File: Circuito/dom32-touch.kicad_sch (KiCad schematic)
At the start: 51 parts, among them J1 MEM2067-02-180-00-A, J2 Poste X 5, J3 MSP3218_LCD, J4 MSP3218_SD, J5 DEBUG, J6 POWER 5v, SW1 TactSwitch, U1 ZLDO1117QG33TADICT-ND, U2 PIC32MM0256GPM028-I-SS

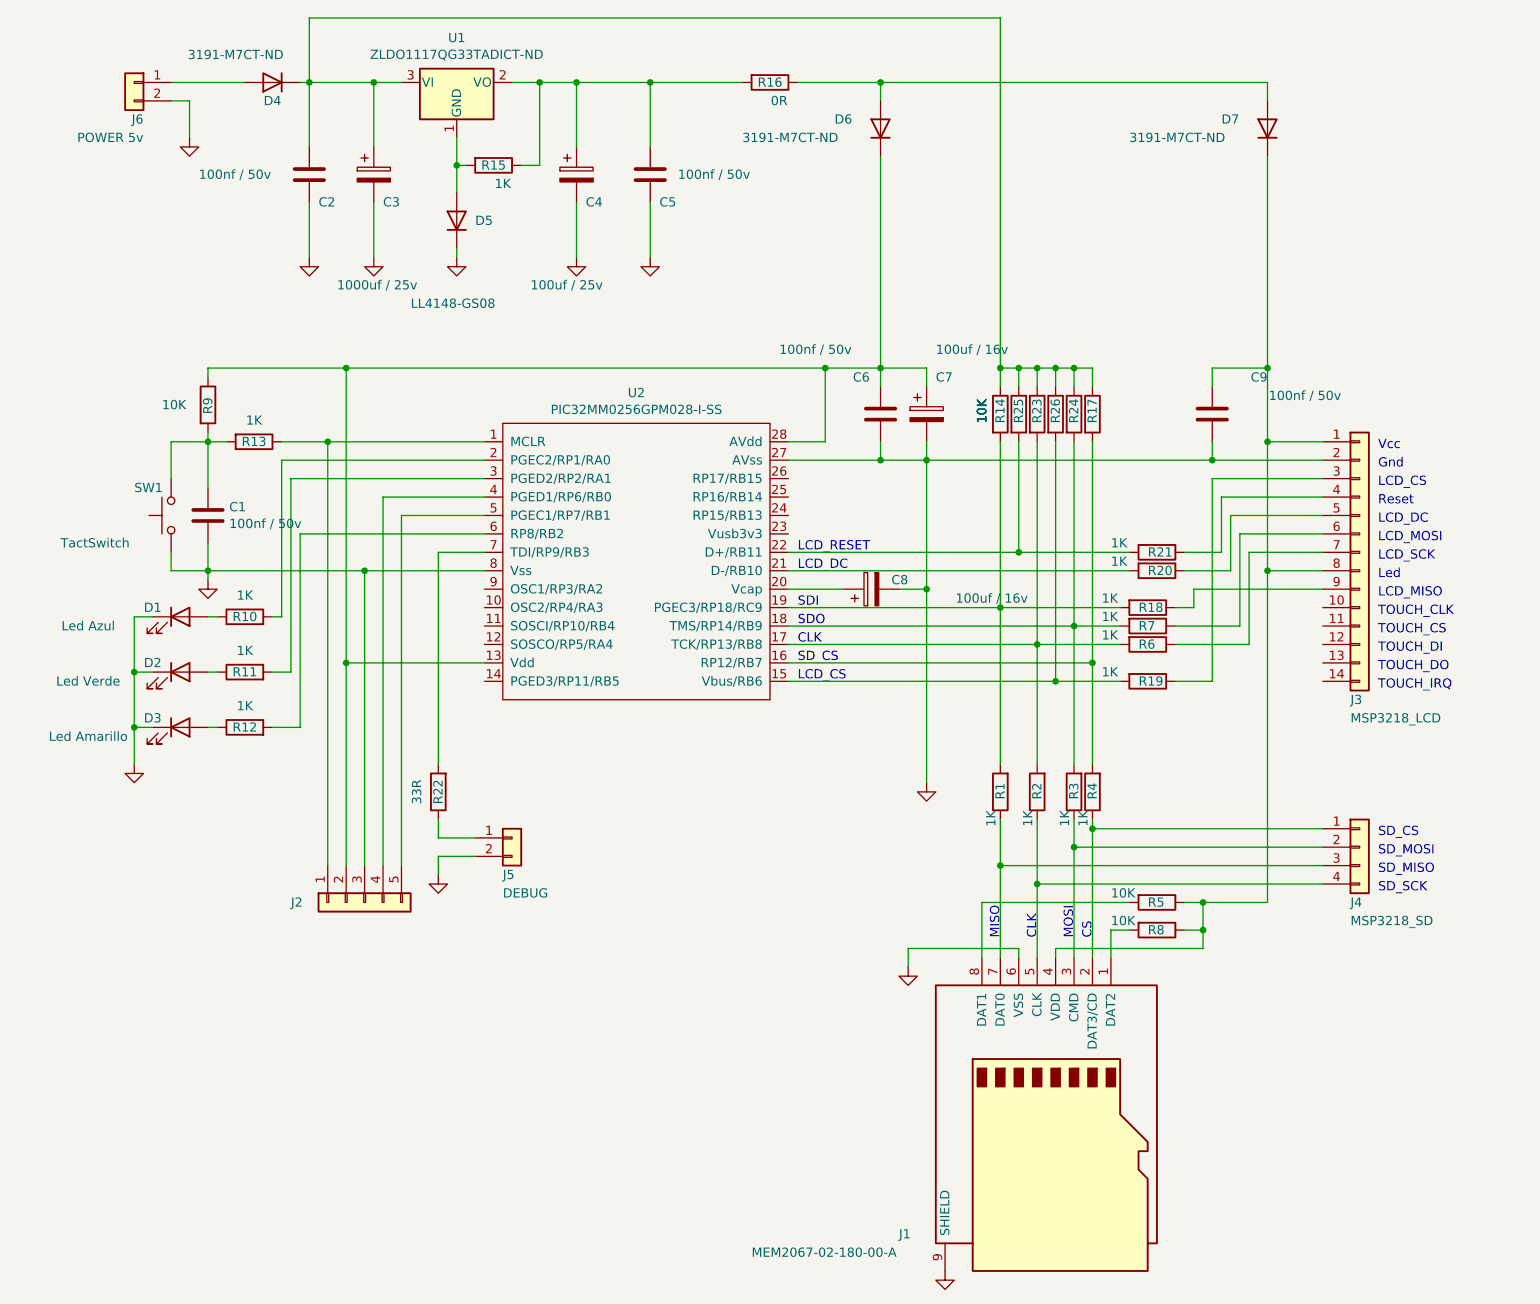
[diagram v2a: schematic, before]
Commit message: Pinta medio display
Pinta medio display
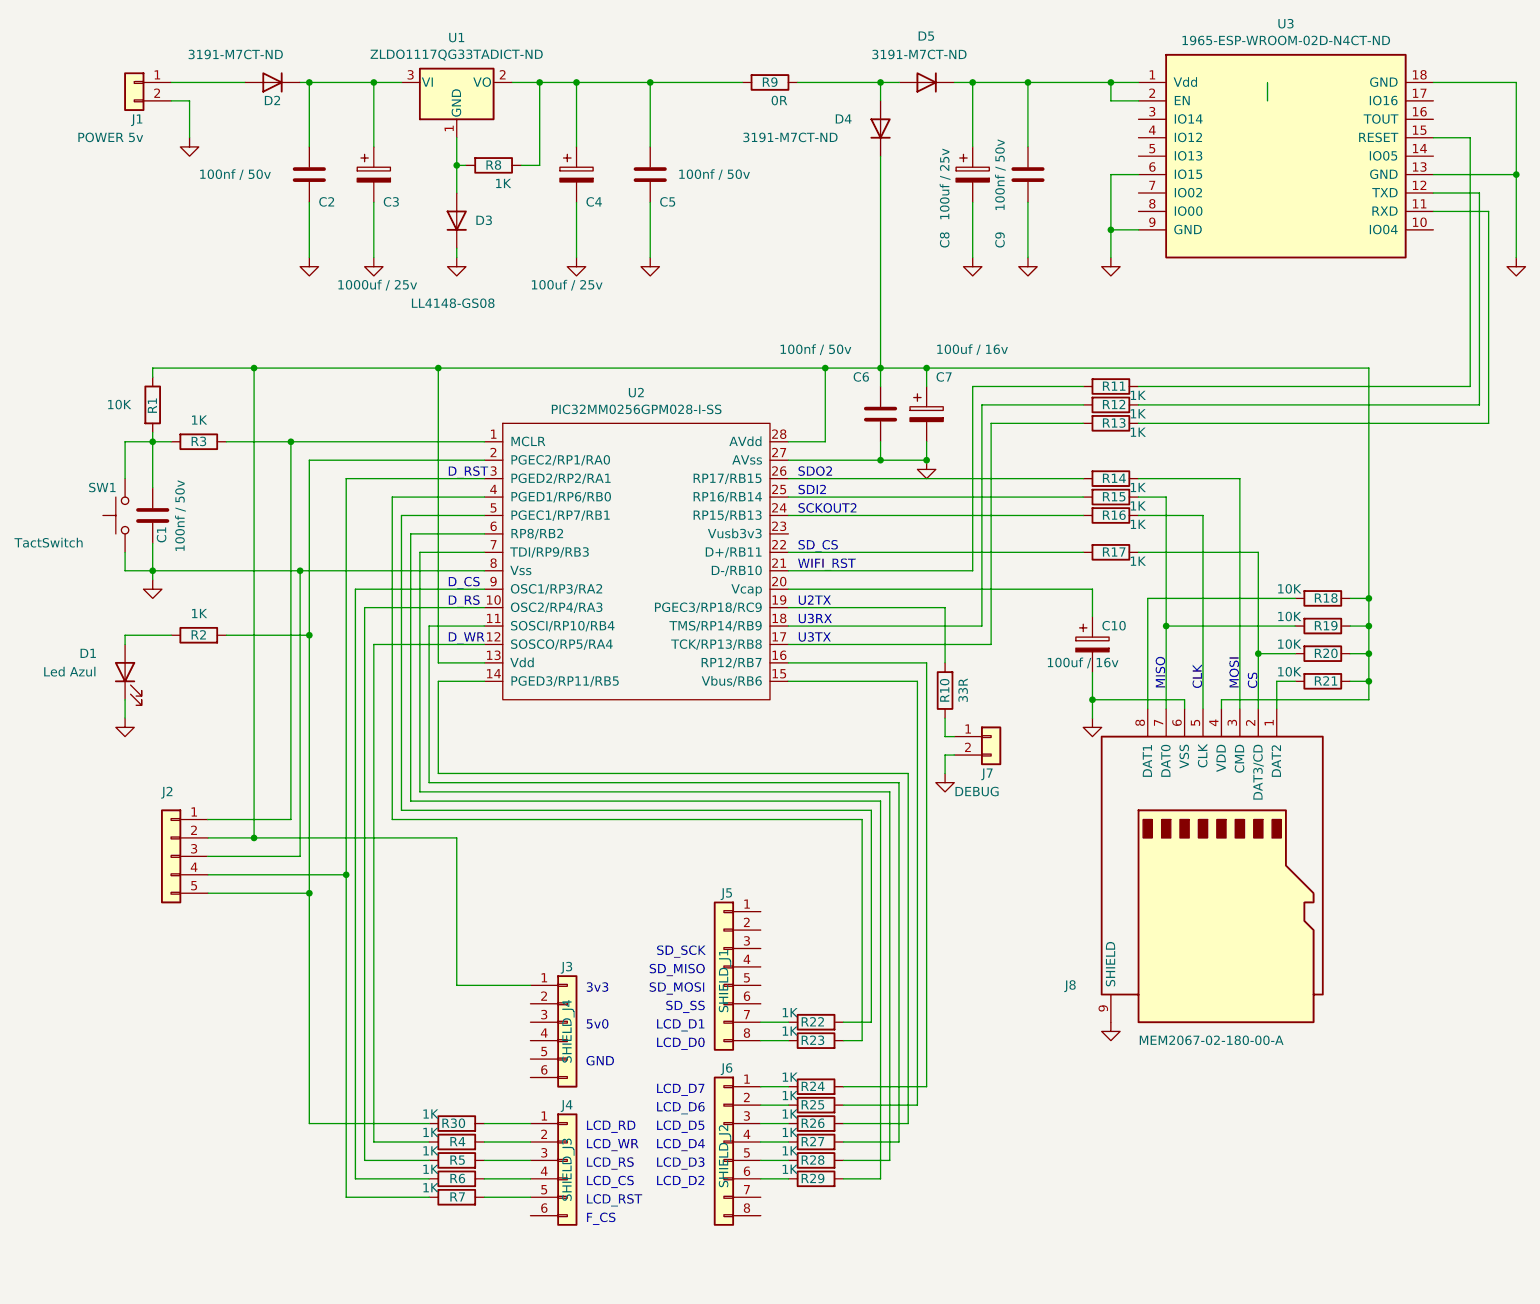
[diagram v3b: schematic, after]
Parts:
- removed D2: Led Verde, Diode_SMD:D_0805_2012Metric_Pad1.15x1.40mm_HandSolder, symbol Device:LED
- removed D3: Led Amarillo, Diode_SMD:D_0805_2012Metric_Pad1.15x1.40mm_HandSolder, symbol Device:LED
- removed D7: 3191-M7CT-ND, Diode_SMD:D_SMA, symbol Device:D
- removed J3: MSP3218_LCD, symbol Connector_Generic:Conn_01x14
- removed J4: MSP3218_SD, symbol Connector_Generic:Conn_01x04
- removed R14, R17: 10K, Resistor_SMD:R_0805_2012Metric_Pad1.20x1.40mm_HandSolder, symbol Device:R
- removed R20, R21: 1K, Resistor_SMD:R_0805_2012Metric_Pad1.20x1.40mm_HandSolder, symbol Device:R
- added C8: 100uf / 25v, Capacitor_THT:CP_Radial_D6.3mm_P2.50mm, symbol Device:C_Polarized
- added D5: 3191-M7CT-ND, Diode_SMD:D_SMA, symbol Device:D
- added J3: SHIELD_J4, symbol Connector_Generic:Conn_01x06
- added J4: SHIELD_J3, symbol Connector_Generic:Conn_01x06
- added J5: SHIELD_J1, symbol Connector_Generic:Conn_01x08
- added J6: SHIELD_J2, symbol Connector_Generic:Conn_01x08
- added R13, R22, R27, R28, R29, R30, R4, R5: 1K, Resistor_SMD:R_0805_2012Metric_Pad1.20x1.40mm_HandSolder, symbol Device:R
- added U3: 1965-ESP-WROOM-02D-N4CT-ND, RF_Module:ESP-WROOM-02, symbol DomIO32-rescue:ESP-02-DomIO32
- R18, R19: value 1K -> 10K
- R23, R24, R25, R26: value 10K -> 1K
- renumbered C8 to C10, D4 to D2, D5 to D3, D6 to D4, J6 to J1, J5 to J7, J1 to J8, R9 to R1, R22 to R10, R3 to R14, R1 to R15, R2 to R16, R4 to R17, R10 to R2, R5 to R20, R8 to R21, R13 to R3, R15 to R8, R16 to R9
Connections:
- net GND: now also C9.2, C8.2, U3.13 (GND), U3.18 (GND), U3.6 (IO15), U3.9 (GND); no longer C9.1
- net at C6.1, C7.1, D4.1 (K)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: now also J8.4 (VDD), R18.1, R19.1, R20.1, R21.1, J3.1 (Pin_1)
- net at J2.4 (Pin_4): now also R7.1, U2.3 (PGED2/RP2/RA1); no longer U2.4 (PGED1/RP6/RB0)
- net at J2.5 (Pin_5): now also R2.2, U2.2 (PGEC2/RP1/RA0), R30.1; no longer U2.5 (PGEC1/RP7/RB1)
- net at C2.1, C3.1, D2.1 (K)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: no longer R23.1, R24.1, R25.1, R26.1
- net at J8.2 (DAT3/CD), R17.1: now also R20.2
- net at J8.7 (DAT0), R15.1: now also R19.2
- net at R17.2: now also U2.22 (D+/RB11); no longer U2.16 (RP12/RB7)
- net at D4.2 (A), R9.1: now also D5.2 (A)
- net at R25.2: now also U2.15 (Vbus/RB6); no longer U2.22 (D+/RB11)
- net at U2.10 (OSC2/RP4/RA3): now also R5.1
- net at U2.11 (SOSCI/RP10/RB4): now also R27.2
- net at U2.12 (SOSCO/RP5/RA4): now also R4.1
- net at U2.14 (PGED3/RP11/RB5): now also R26.2
- net at U2.21 (D-/RB10): now also R11.2
- net at U2.24 (RP15/RB13): now also R16.2
- net at U2.25 (RP16/RB14): now also R15.2
- net at U2.26 (RP17/RB15): now also R14.2
- net at R12.2: now also U2.18 (TMS/RP14/RB9); no longer U2.6 (RP8/RB2)
- net at R10.2: now also U2.19 (PGEC3/RP18/RC9); no longer U2.7 (TDI/RP9/RB3)
- net at U2.9 (OSC1/RP3/RA2): now also R6.1
- net at J8.8 (DAT1): now also R18.2; no longer R20.2
- net at R11.1: now also U3.15 (RESET)
- net at R12.1: now also U3.12 (TXD)
- new net: J6.2 (Pin_2), R25.1
- new net: C8.1, C9.1, D5.1 (K), U3.1 (Vdd), U3.2 (EN)
- new net: J6.1 (Pin_1), R24.1
- new net: J6.3 (Pin_3), R26.1
- new net: J6.4 (Pin_4), R27.1
- new net: J6.5 (Pin_5), R28.1
- new net: J6.6 (Pin_6), R29.1
- new net: J4.5 (Pin_5), R7.2
- new net: R24.2, U2.16 (RP12/RB7)
- new net: R13.2, U2.17 (TCK/RP13/RB8)
- new net: R23.2, U2.4 (PGED1/RP6/RB0)
- new net: R22.2, U2.5 (PGEC1/RP7/RB1)
- new net: R29.2, U2.6 (RP8/RB2)
- new net: R28.2, U2.7 (TDI/RP9/RB3)
- new net: J5.8 (Pin_8), R23.1
- new net: J4.1 (Pin_1), R30.2
- new net: J4.2 (Pin_2), R4.2
- new net: J4.3 (Pin_3), R5.2
- new net: J4.4 (Pin_4), R6.2
- new net: R13.1, U3.11 (RXD)
- new net: J5.7 (Pin_7), R22.1
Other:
- note added: "3v3"
- note added: "5v0"
- note added: "D_CS"
- note added: "D_RS"
- note added: "D_RST"
- note added: "D_WR"
- note added: "F_CS"
- note added: "GND"
- note added: "LCD_D0"
- note added: "LCD_D1"
- note added: "LCD_D2"
- note added: "LCD_D3"
- note added: "LCD_D4"
- note added: "LCD_D5"
- note added: "LCD_D6"
- note added: "LCD_D7"
- note added: "LCD_RD"
- note added: "LCD_RS"
- note added: "LCD_RST"
- note added: "LCD_WR"
- note added: "SCKOUT2"
- note added: "SDI2"
- note added: "SDO2"
- note added: "SD_SS"
- note added: "U2TX"
- note added: "U3RX"
- note added: "U3TX"
- note added: "WIFI_RST"
- note removed: "Gnd"
- note removed: "LCD_DC"
- note removed: "LCD_MISO"
- note removed: "LCD_MOSI"
- note removed: "LCD_RESET"
- note removed: "LCD_SCK"
- note removed: "Led"
- note removed: "Reset"
- note removed: "SDI"
- note removed: "SDO"
- note removed: "TOUCH_CLK"
- note removed: "TOUCH_CS"
- note removed: "TOUCH_DI"
- note removed: "TOUCH_DO"
- note removed: "TOUCH_IRQ"
- note removed: "Vcc"
- moved on the sheet: C1, C10, D1, J2, J7, J8, R1, R10, R14, R15, R16, R17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

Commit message: Texto
Texto
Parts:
- removed R22, R23, R24, R25, R26, R27, R28, R29, R30, R4, R5, R6, R7: 1K, Resistor_SMD:R_0805_2012Metric_Pad1.20x1.40mm_HandSolder, symbol Device:R
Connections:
- net at J6.2 (Pin_2): now also U2.15 (Vbus/RB6)
- net at J2.4 (Pin_4), U2.3 (PGED2/RP2/RA1): now also J4.5 (Pin_5)
- net at J2.5 (Pin_5), R2.2, U2.2 (PGEC2/RP1/RA0): now also J4.1 (Pin_1)
- net at J6.1 (Pin_1): now also U2.16 (RP12/RB7)
- net at J6.3 (Pin_3): now also U2.14 (PGED3/RP11/RB5)
- net at J6.4 (Pin_4): now also U2.11 (SOSCI/RP10/RB4)
- net at J6.5 (Pin_5): now also U2.7 (TDI/RP9/RB3)
- net at J6.6 (Pin_6): now also U2.6 (RP8/RB2)
- net at R17.2, U2.22 (D+/RB11): now also J5.6 (Pin_6)
- net at R15.2, U2.25 (RP16/RB14): now also J5.4 (Pin_4)
- net at R14.2, U2.26 (RP17/RB15): now also J5.5 (Pin_5)
- net at U2.10 (OSC2/RP4/RA3): now also J4.3 (Pin_3)
- net at U2.12 (SOSCO/RP5/RA4): now also J4.2 (Pin_2)
- net at R16.2, U2.24 (RP15/RB13): now also J5.3 (Pin_3)
- net at U2.4 (PGED1/RP6/RB0): now also J5.8 (Pin_8)
- net at U2.5 (PGEC1/RP7/RB1): now also J5.7 (Pin_7)
- net at U2.9 (OSC1/RP3/RA2): now also J4.4 (Pin_4)
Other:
- note added: "D_RD"
- moved on the sheet: C1, C10, J2, J7, R10, R11, R12, R13, R14, R15, R16, R17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

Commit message: Boton con icono
Boton con icono
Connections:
- net GND: now also J3.5 (Pin_5)
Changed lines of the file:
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@@
+    (stroke (width 0) (type default))
+  )
+  (wire (pts (xy 87.63 163.83) (xy 85.09 163.83))
     (stroke (width 0) (type default))
   )
@@
   )
   (wire (pts (xy 198.12 115.57) (xy 198.12 114.3))
+    (stroke (width 0) (type default))
+  )
+  (wire (pts (xy 85.09 163.83) (xy 85.09 167.64))
     (stroke (width 0) (type default))
   )
@@
         )
       )
+    )
+  )
+  (symbol (lib_id "power:GND") (at 85.09 167.64 0) (unit 1)
+    (in_bom yes) (on_board yes) (dnp no)
+    (property "Reference" "#PWR017" (at 85.09 173.99 0)
+      (effects (font (size 1.27 1.27)) hide)
+    )
+    (property "Value" "GND" (at 85.217 172.0342 0)
+      (effects (font (size 1.27 1.27)) hide)
+    )
+    (property "Footprint" "" (at 85.09 167.64 0)
+      (effects (font (size 1.27 1.27)) hide)
+    )
+    (property "Datasheet" "" (at 85.09 167.64 0)
+      (effects (font (size 1.27 1.27)) hide)
+    )
+    (pin "1")
+    (instances
+      (project "dom32-touch"
+        (path "/52c02980-b5ea-450b-8d27-915fdca3d27d"
+          (reference "#PWR017") (unit 1)
+        )
+      )

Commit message: Agregado de modulo wifi
Agregado de modulo wifi
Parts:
- removed D1: Led Azul, Diode_SMD:D_0805_2012Metric_Pad1.15x1.40mm_HandSolder, symbol Device:LED
- removed J3: SHIELD_J4, symbol Connector_Generic:Conn_01x06
- removed J4: SHIELD_J3, symbol Connector_Generic:Conn_01x06
- removed J5: SHIELD_J1, symbol Connector_Generic:Conn_01x08
- removed J6: SHIELD_J2, symbol Connector_Generic:Conn_01x08
- removed R2: 1K, Resistor_SMD:R_0805_2012Metric_Pad1.20x1.40mm_HandSolder, symbol Device:R
- added J3: CF4240FH0R0-05-NH, Connector_FFC-FPC:TE_4-1734839-0_1x40-1MP_P0.5mm_Horizontal, symbol Connector_Generic:Conn_01x40
- added Q1: BC548, Package_TO_SOT_THT:TO-92_Inline, symbol Transistor_BJT:BC548
- added R3: 10K, Resistor_SMD:R_0805_2012Metric_Pad1.20x1.40mm_HandSolder, symbol Device:R
- J2: renamed from J1; footprint (none) -> TerminalBlock_Phoenix:TerminalBlock_Phoenix_PT-1,5-2-5.0-H_1x02_P5.00mm_Horizontal
- J4: renamed from J7; value DEBUG -> DEBUG & Buzzer; footprint (none) -> Connector_PinHeader_2.54mm:PinHeader_1x02_P2.54mm_Vertical
- renumbered D2 to D1, D3 to D2, D4 to D3, D5 to D4, J2 to J1, J8 to J5, R14 to R10, R15 to R11, R16 to R12, R17 to R13, R18 to R14, R19 to R15, R20 to R16, R21 to R17, R3 to R2, R8 to R4, R9 to R5, R10 to R6, R11 to R7, R12 to R8, R13 to R9
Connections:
- net GND: now also J3.14 (Pin_14), J3.15 (Pin_15), J3.16 (Pin_16), J3.17 (Pin_17), J3.18 (Pin_18), J3.19 (Pin_19), J3.20 (Pin_20), J3.21 (Pin_21), J3.22 (Pin_22), J3.23 (Pin_23), J3.24 (Pin_24), J3.3 (Pin_3), Q1.3 (E)
- net at C6.1, C7.1, D3.1 (K)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: now also J3.12 (Pin_12), J3.2 (Pin_2), J3.33 (Pin_33)
- net at J1.4 (Pin_4), U2.3 (PGED2/RP2/RA1): now also J3.13 (Pin_13)
- net at J1.5 (Pin_5), U2.2 (PGEC2/RP1/RA0): now also R3.1
- net at U2.16 (RP12/RB7): now also J3.25 (Pin_25), J3.38 (Pin_38)
- net at U2.15 (Vbus/RB6): now also J3.26 (Pin_26), J3.37 (Pin_37)
- net at U2.14 (PGED3/RP11/RB5): now also J3.27 (Pin_27)
- net at U2.11 (SOSCI/RP10/RB4): now also J3.28 (Pin_28)
- net at U2.7 (TDI/RP9/RB3): now also J3.29 (Pin_29)
- net at U2.6 (RP8/RB2): now also J3.30 (Pin_30)
- net at U2.10 (OSC2/RP4/RA3): now also J3.35 (Pin_35), J3.39 (Pin_39)
- net at U2.12 (SOSCO/RP5/RA4): now also J3.34 (Pin_34), J3.40 (Pin_40)
- net at U2.4 (PGED1/RP6/RB0): now also J3.32 (Pin_32)
- net at U2.5 (PGEC1/RP7/RB1): now also J3.31 (Pin_31)
- net at U2.9 (OSC1/RP3/RA2): now also J3.36 (Pin_36)
- new net: J3.1 (Pin_1), Q1.1 (C)
- new net: Q1.2 (B), R3.2
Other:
- note added: "DB0"
- note added: "DB1"
- note added: "DB10"
- note added: "DB11"
- note added: "DB12"
- note added: "DB13"
- note added: "DB14"
- note added: "DB15"
- note added: "DB16"
- note added: "DB17"
- note added: "DB2"
- note added: "DB3"
- note added: "DB4"
- note added: "DB5"
- note added: "DB6"
- note added: "DB7"
- note added: "DB8"
- note added: "DB9"
- note added: "DE"
- note added: "DOT_CLK"
- note added: "D_BKL"
- note added: "Display: AFY240320B0-2.4N6NTM-R"
- note added: "HSYNC"
- note added: "LED_A"
- note added: "LED_K"
- note added: "NC"
- note added: "RD"
- note added: "RESET"
- note added: "RS"
- note added: "SDA"
- note added: "VCC"
- note added: "VSYNC"
- note added: "WR"
- note added: "XL"
- note added: "XR"
- note added: "YD"
- note added: "YU"
- note removed: "3v3"
- note removed: "5v0"
- note removed: "D_RD"
- note removed: "F_CS"
- note removed: "LCD_RD"
- note removed: "SD_MISO"
- note removed: "SD_MOSI"
- note removed: "SD_SCK"
- note removed: "SD_SS"
- moved on the sheet: J1
